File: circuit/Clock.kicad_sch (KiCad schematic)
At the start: 12 parts, among them U1 WeMos_S2_mini

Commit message: updated to be gooderer
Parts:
- added C1: 100nF, Capacitor_THT:C_Disc_D8.0mm_W2.5mm_P5.00mm, symbol Device:C
- renumbered R1 to 10kΩ1
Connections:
- net Ground: now also C1.2
- net MinusSignal: now reaches Minus1.2 (Pin_2), U1.5 (GPIO9)
- net Power: now reaches 10kΩ1.1, Circle1.3 (Pin_3), Display1.5 (Pin_5), Minus1.3 (Pin_3), Plus1.3 (Pin_3), Triangle1.3 (Pin_3), U1.8 (3V3)
- net Power: now also C1.1
- net DisplaySignal: now reaches Display1.3 (Pin_3), U1.14 (GPIO35)
- net PhotoresistorSignal: now reaches U1.17 (GPIO1)
- net PhotoresistorSignal: now also 10kΩ1.2, R2.1
- net CS: now reaches Display1.2 (Pin_2), U1.29 (GPIO34)
- net TriangleSignal: now reaches Triangle1.2 (Pin_2), U1.3 (GPIO5)
- net Clock: now reaches Display1.1 (Pin_1), U1.30 (GPIO36)
- net CircleSignal: now reaches Circle1.2 (Pin_2), U1.4 (GPIO7)
- net PlusSignal: now reaches Plus1.2 (Pin_2), U1.6 (GPIO11)
- now unconnected: U1.32 (GPIO40)
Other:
- moved on the sheet: 10kΩ1, Circle1, Display1, H1, H2, H3, H4, Minus1, Plus1, R2, Triangle1

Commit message: rev 1.0 of pcb
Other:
- moved on the sheet: C1
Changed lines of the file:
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@@
+	(wire
+		(pts
+			(xy 163.83 104.14) (xy 163.83 124.46)
+		)
+		(stroke
+			(width 0)
+			(type default)
+		)
+	)
 	(wire
 		(pts
@@
 	(wire
 		(pts
-			(xy 128.27 124.46) (xy 161.29 124.46)
+			(xy 128.27 124.46) (xy 163.83 124.46)
 		)
 		(stroke
@@
 	(wire
 		(pts
-			(xy 161.29 124.46) (xy 181.61 104.14)
-		)
-		(stroke
-			(width 0)
-			(type default)
-		)
-	)
-	(wire
-		(pts
 			(xy 25.4 48.26) (xy 52.07 48.26)
 		)
@@
 	(wire
 		(pts
-			(xy 181.61 53.34) (xy 181.61 96.52)
+			(xy 163.83 53.34) (xy 163.83 96.52)
 		)
 		(stroke
@@
 	(wire
 		(pts
-			(xy 133.35 53.34) (xy 181.61 53.34)
+			(xy 133.35 53.34) (xy 163.83 53.34)
 		)
 		(stroke
@@
 		(on_board yes)
 		(dnp no)
-		(fields_autoplaced yes)
 		(property "Reference" "Minus1"
-			(at 40.005 52.07 0)
+			(at 39.37 54.356 0)
 			(effects
 				(font
@@
 		)
 		(property "Value" "Conn_01x03_Pin"
-			(at 40.005 54.61 0)
+			(at 38.735 52.324 0)
 			(effects
 				(font
@@
 	(symbol
 		(lib_id "Device:C")
-		(at 181.61 100.33 0)
+		(at 163.83 100.33 0)
 		(unit 1)
 		(exclude_from_sim no)
@@
 		(fields_autoplaced yes)
 		(property "Reference" "C1"
-			(at 185.42 99.0599 0)
+			(at 167.64 99.0599 0)
 			(effects
 				(font
@@
 		)
 		(property "Value" "100nF"
-			(at 185.42 101.5999 0)
+			(at 167.64 101.5999 0)
 			(effects
 				(font
@@
 		)
 		(property "Footprint" "Capacitor_THT:C_Disc_D8.0mm_W2.5mm_P5.00mm"
-			(at 182.5752 104.14 0)
+			(at 164.7952 104.14 0)
 			(effects
 				(font
@@
 		)
 		(property "Datasheet" "~"
-			(at 181.61 100.33 0)
+			(at 163.83 100.33 0)
 			(effects
 				(font
@@
 		)
 		(property "Description" "Unpolarized capacitor"
-			(at 181.61 100.33 0)
+			(at 163.83 100.33 0)
 			(effects
 				(font
@@
 		(dnp no)
 		(property "Reference" "Plus1"
-			(at 40.005 31.75 0)
+			(at 39.624 34.29 0)
 			(effects
 				(font
@@
 		)
 		(property "Value" "Conn_01x03_Pin"
-			(at 40.005 34.29 0)
+			(at 38.989 32.258 0)
 			(effects
 				(font
@@
 		(on_board yes)
 		(dnp no)
-		(fields_autoplaced yes)
 		(property "Reference" "Circle1"
-			(at 42.545 69.85 0)
+			(at 41.91 72.39 0)
 			(effects
 				(font
@@
 		)
 		(property "Value" "Conn_01x03_Pin"
-			(at 42.545 72.39 0)
+			(at 41.91 70.358 0)
 			(effects
 				(font
@@
 		(on_board yes)
 		(dnp no)
-		(fields_autoplaced yes)
 		(property "Reference" "Display1"
-			(at 40.005 100.33 0)
+			(at 39.37 103.124 0)
 			(effects
 				(font
@@
 		)
 		(property "Value" "Conn_01x05_Pin"
-			(at 40.005 102.87 0)
+			(at 39.37 101.346 0)
 			(effects
 				(font
@@
 		(dnp no)
 		(property "Reference" "Triangle1"
-			(at 41.91 85.09 0)
+			(at 41.91 87.884 0)
 			(effects
 				(font
@@
 		)
 		(property "Value" "Conn_01x03_Pin"
-			(at 42.545 87.63 0)
+			(at 41.91 85.852 0)
 			(effects
 				(font
@@
 		(on_board yes)
 		(dnp no)
-		(fields_autoplaced yes)
 		(property "Reference" "10kΩ1"
-			(at 66.04 153.6699 0)
+			(at 65.278 155.702 0)
 			(effects
 				(font
@@
 		)
 		(property "Value" "R"
-			(at 66.04 156.2099 0)
-			(effects
-				(font
+			(at 65.278 153.924 0)
+			(effects
+				(font

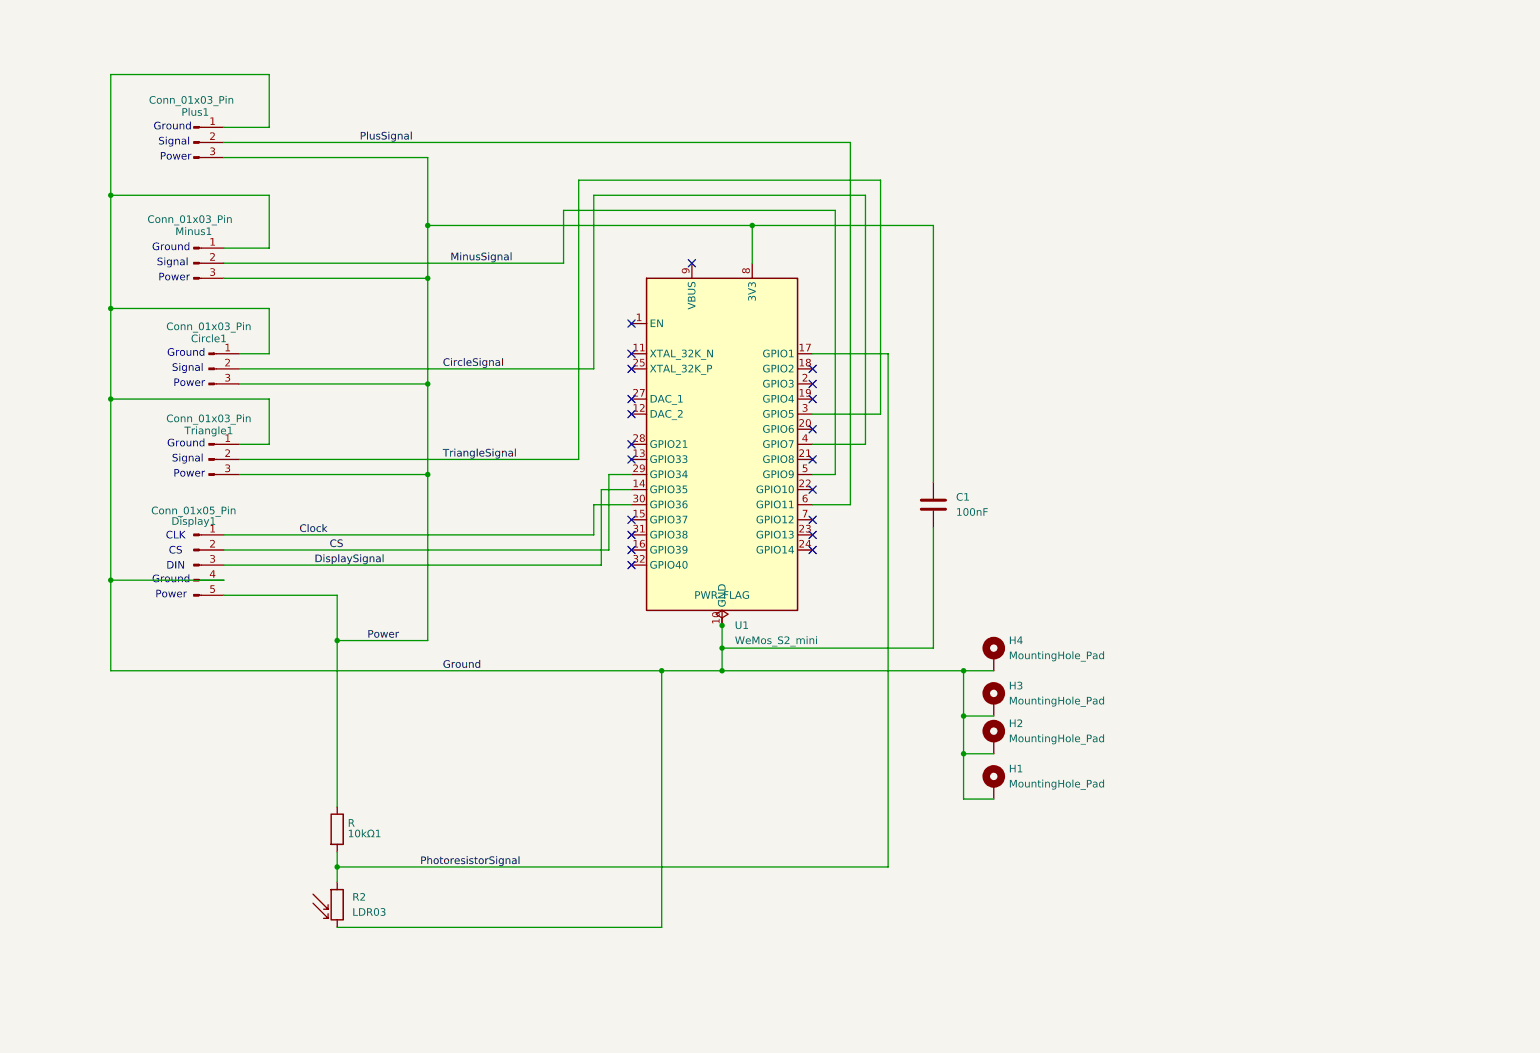
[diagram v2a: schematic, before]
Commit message: Update Clock PCB nets & footprints
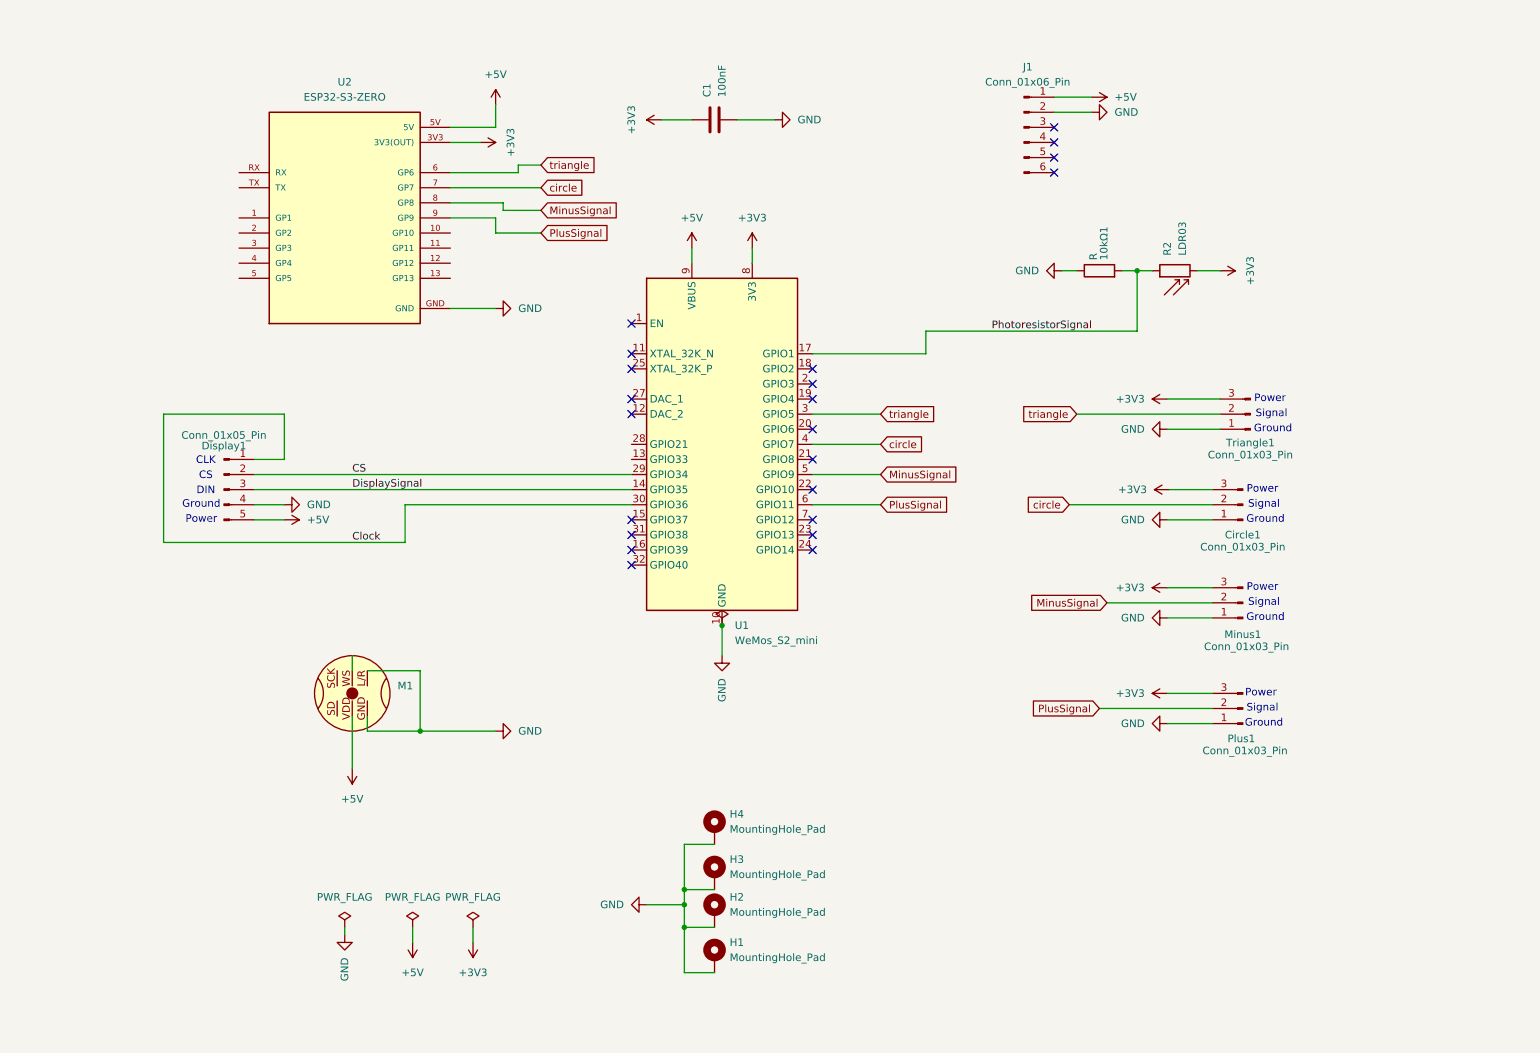
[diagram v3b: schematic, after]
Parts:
- added J1: Conn_01x06_Pin, Connector_PinHeader_2.54mm:PinHeader_1x06_P2.54mm_Vertical, symbol Connector:Conn_01x06_Pin
- added M1: ~, Library:INMP441, symbol custom:INMP441_Microphone_I2S
- added U2: ESP32-S3-ZERO, waveshare:MODULE_ESP32-S3-ZERO, symbol esp32zero:ESP32-S3-ZERO
- U1: footprint wemos2:wemoss2 -> Module:WEMOS_S2_mini
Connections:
- net MinusSignal: now also U2.8 (GP8)
- net PlusSignal: now also U2.9 (GP9)
- net +5V: now reaches U1.9 (VBUS)
- net +5V: now also Display1.5 (Pin_5), J1.1 (Pin_1), M1.VDD, U2.5V
- net CircleSignal renamed circle
- net circle: now also U2.7 (GP7)
- net Ground renamed GND
- net GND: now also 10kΩ1.1, J1.2 (Pin_2), M1.GND, M1.L/R, U2.GND; no longer R2.2
- net Power renamed +3V3
- net +3V3: now also R2.2, U2.3V3 (3V3(OUT)); no longer 10kΩ1.1, Display1.5 (Pin_5)
- net TriangleSignal renamed triangle
- net triangle: now also U2.6 (GP6)
- no-connect marks 21 -> 22
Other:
- moved on the sheet: 10kΩ1, C1, Circle1, Display1, H1, H2, H3, H4, Minus1, Plus1, R2, Triangle1

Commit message: updated pcb
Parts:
- added C2: 100nF, Capacitor_THT:C_Disc_D8.0mm_W2.5mm_P5.00mm, symbol Device:C
- U1: footprint Module:WEMOS_S2_mini -> wemos2:wemoss2
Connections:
- net +5V: now also C2.1
- net CS: now also U2.3 (GP3)
- net Clock: now also U2.2 (GP2)
- net DisplaySignal: now also U2.4 (GP4)
- net GND: now also C2.2
- net PhotoresistorSignal: now also U2.10 (GP10)
- net SD: now reaches U2.11 (GP11)
- net SD: now also M1.SD
- net SCK: now reaches U2.12 (GP12)
- net SCK: now also M1.SCK
- net WS: now reaches U2.13 (GP13)
- net WS: now also M1.WS
- no-connect marks 22 -> 28
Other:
- moved on the sheet: 10kΩ1, C1, Circle1, H1, H2, H3, H4, J1, M1, Minus1, Plus1, R2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

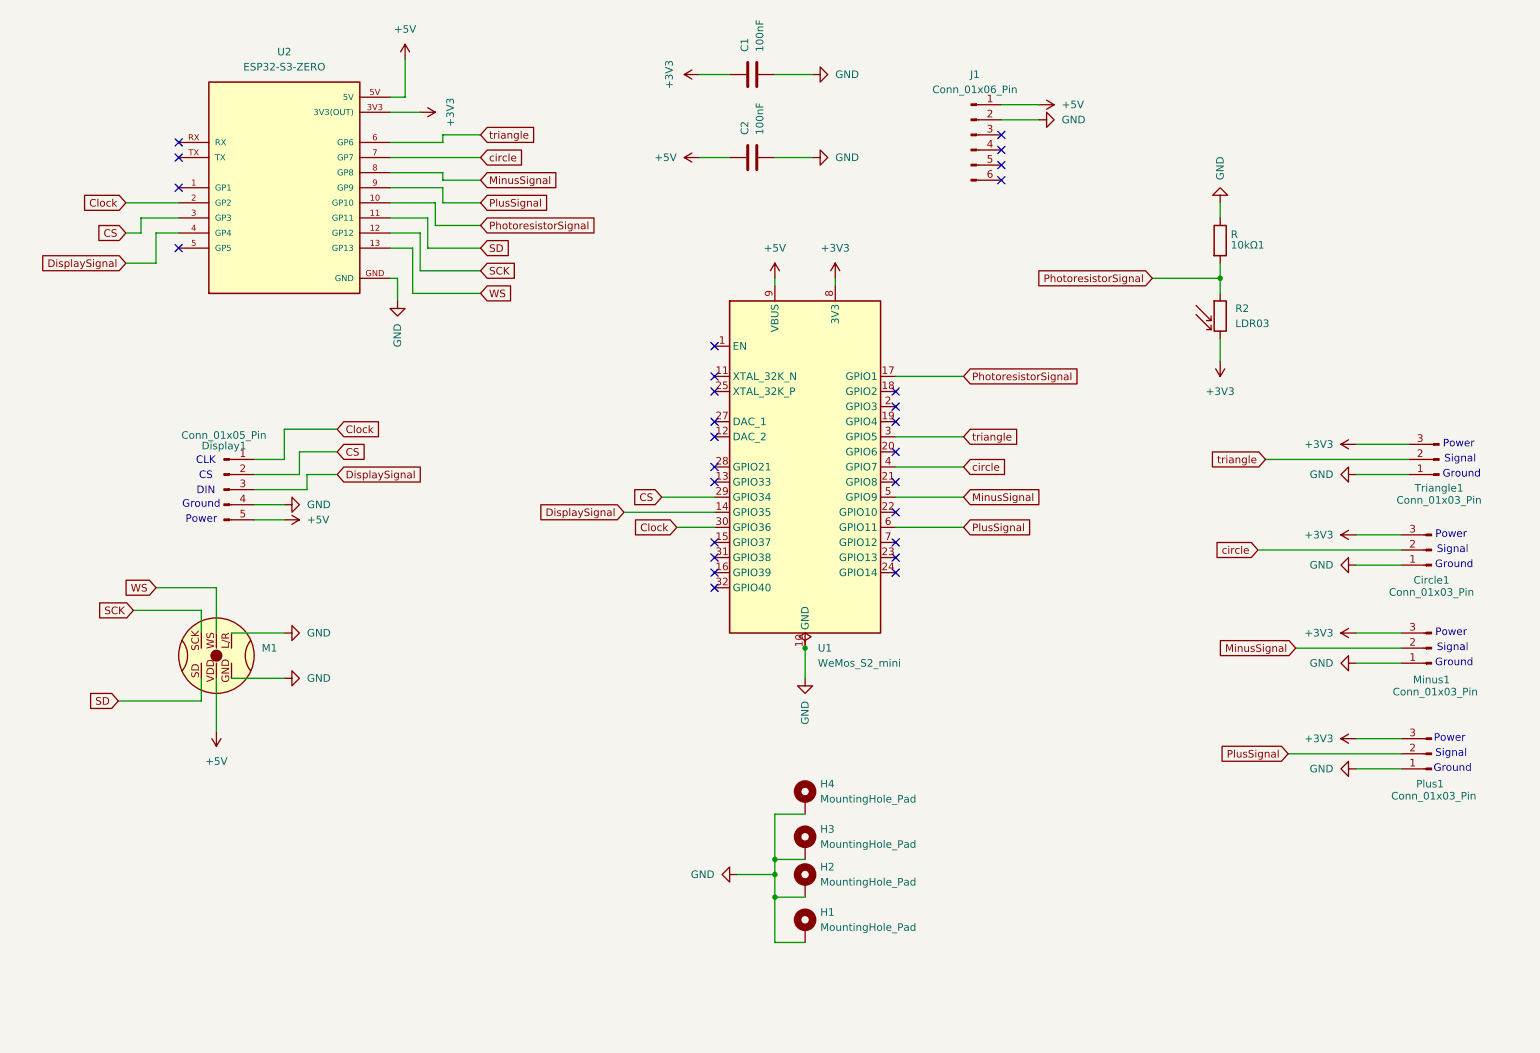
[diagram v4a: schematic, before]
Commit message: ESPHome config now works - needed two I2S channels for input/output. Updated circuit design to reflect this, and better designed PCB/layout with updated ESPS3-zero footprint/symbol
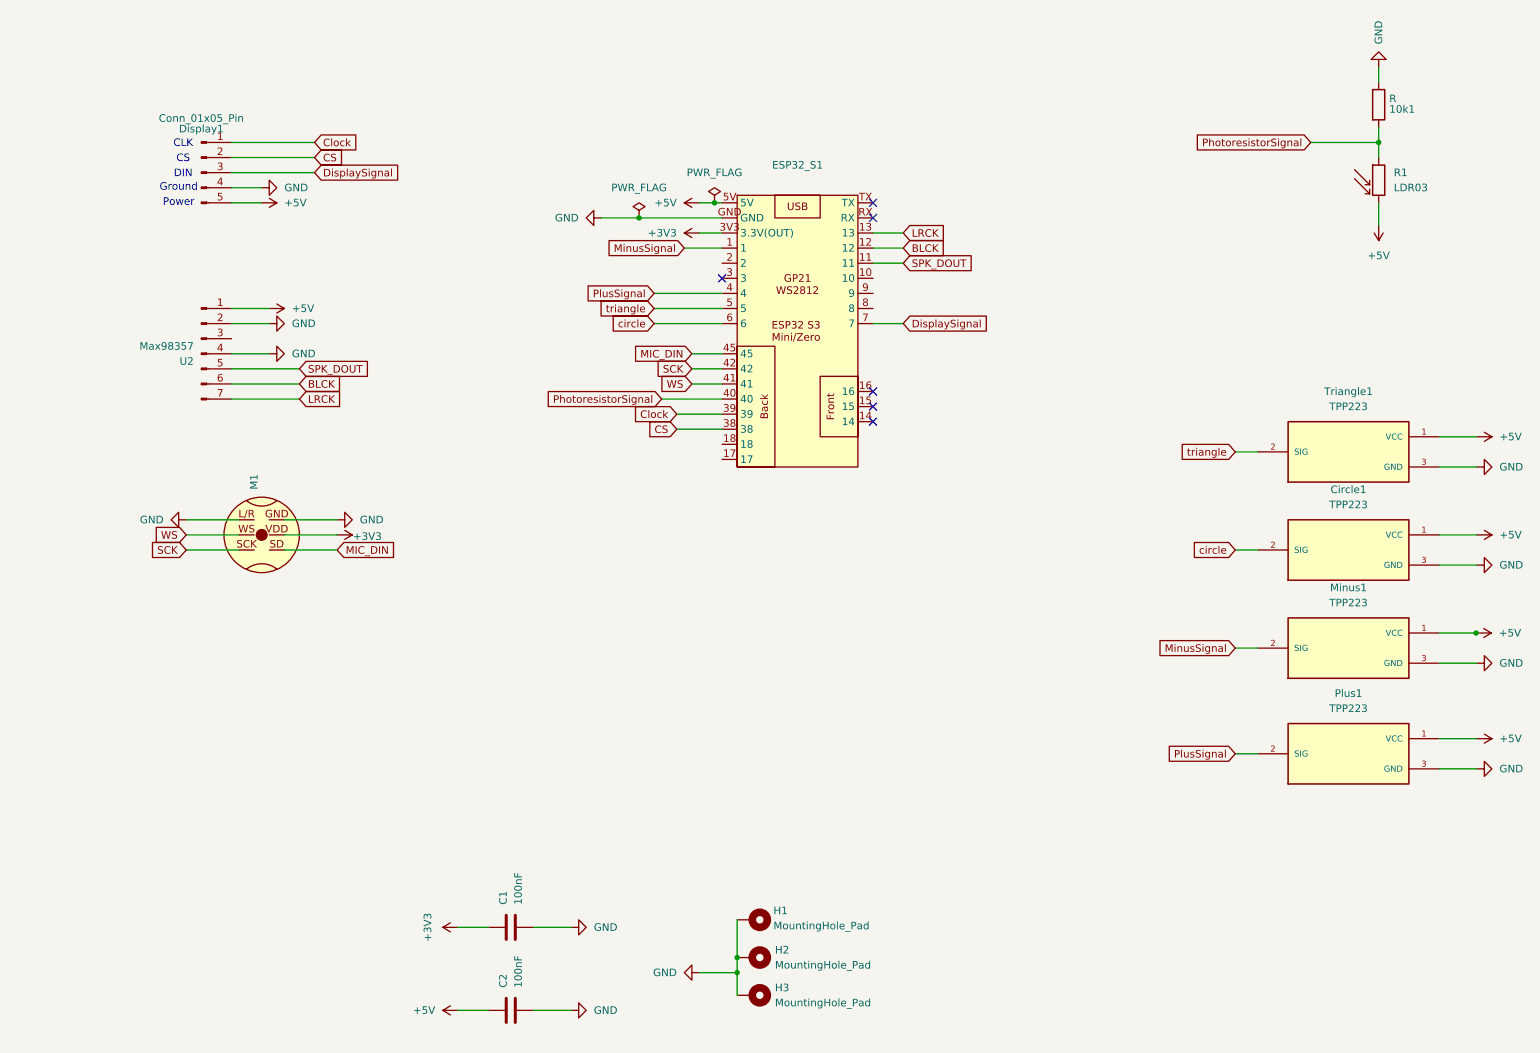
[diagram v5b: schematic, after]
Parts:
- removed Circle1, Minus1, Plus1, Triangle1: Conn_01x03_Pin, Connector_PinHeader_2.54mm:PinHeader_1x03_P2.54mm_Vertical, symbol Connector:Conn_01x03_Pin
- removed H1: MountingHole_Pad, MountingHole:MountingHole_3.2mm_M3_Pad, symbol Mechanical:MountingHole_Pad
- removed J1: Conn_01x06_Pin, Connector_PinHeader_2.54mm:PinHeader_1x06_P2.54mm_Vertical, symbol Connector:Conn_01x06_Pin
- removed U1: WeMos_S2_mini, wemos2:wemoss2, symbol wemos2:WeMos_S2_mini
- removed U2: ESP32-S3-ZERO, waveshare:MODULE_ESP32-S3-ZERO, symbol esp32zero:ESP32-S3-ZERO
- added Circle1, Minus1, Plus1, Triangle1: TPP223, Connector_PinHeader_2.54mm:PinHeader_1x03_P2.54mm_Vertical, symbol PaulsCoolKicadLibrary:TPP223
- added ESP32_S1: ~, PaulsCoolKicadLibrary:MODULE_ESP32-S3-ZERO, symbol Pauls Kicad Lib:Waveshare_ESP32_S3_Mini_Zero
- added U2: Max98357, Connector_PinHeader_2.54mm:PinHeader_1x07_P2.54mm_Vertical, symbol Connector:Conn_01x07_Pin
- Display1: footprint Connector_PinHeader_2.54mm:PinHeader_1x05_P2.54mm_Vertical -> Connector_PinSocket_2.54mm:PinSocket_1x05_P2.54mm_Vertical
- M1: footprint Library:INMP441 -> PaulsCoolKicadLibrary:INMP441
- renumbered 10kΩ1 to 10k1, H4 to H1, H3 to H2, H2 to H3, R2 to R1
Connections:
- net +3V3: now also M1.VDD, ESP32_S1.3V3 (3.3V(OUT)); no longer R1.2
- net +5V: now also R1.2, Circle1.1 (VCC), ESP32_S1.5V, Minus1.1 (VCC), Plus1.1 (VCC), Triangle1.1 (VCC), U2.1 (Pin_1); no longer M1.VDD
- net CS: now also ESP32_S1.38
- net Clock: now also ESP32_S1.39
- net DisplaySignal: now also ESP32_S1.7
- net GND: now also Circle1.3 (GND), ESP32_S1.GND, Minus1.3 (GND), Plus1.3 (GND), Triangle1.3 (GND), U2.2 (Pin_2), U2.4 (Pin_4)
- net MinusSignal: now also ESP32_S1.1, Minus1.2 (SIG)
- net PhotoresistorSignal: now also ESP32_S1.40
- net PlusSignal: now also ESP32_S1.4, Plus1.2 (SIG)
- net SCK: now also ESP32_S1.42
- net WS: now also ESP32_S1.41
- net circle: now also Circle1.2 (SIG), ESP32_S1.6
- net triangle: now also ESP32_S1.5, Triangle1.2 (SIG)
- net SD renamed MIC_DIN
- net MIC_DIN: now also ESP32_S1.45
- new net BLCK: ESP32_S1.12, U2.6 (Pin_6)
- new net LRCK: ESP32_S1.13, U2.7 (Pin_7)
- new net SPK_DOUT: ESP32_S1.11, U2.5 (Pin_5)
- no-connect marks 28 -> 6
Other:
- note removed: "Signal"
- moved on the sheet: 10k1, C1, C2, Display1, H1, H2, H3, M1, R1

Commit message: more tweaks
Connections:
- net MIC_DIN: now also ESP32_S1.40; no longer ESP32_S1.45
- net PhotoresistorSignal: now also ESP32_S1.41; no longer ESP32_S1.40
- net SCK: now also ESP32_S1.45; no longer ESP32_S1.42
- net WS: now also ESP32_S1.42; no longer ESP32_S1.41
